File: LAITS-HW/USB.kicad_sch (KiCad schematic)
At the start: 27 parts, among them J201 USB_C_Receptacle_USB2.0, Q201 PDTC114Y, Q202 PDTC114Y, Q203 NX7002AK, Q204 NX7002AK, U201 CP2102N-Axx-xQFN28

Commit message: generate IBOM
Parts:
- Q203, Q204: Place (none) -> DNP; Status DNP -> (none)
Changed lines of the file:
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@@
       (effects (font (size 1.27 1.27)) hide)
     )
-    (property "Status" "DNP" (id 4) (at 274.955 123.19 0))
+    (property "Place" "DNP" (id 4) (at 274.955 123.19 0))
     (pin "1")
     (pin "2")
@@
       (effects (font (size 1.27 1.27)) hide)
     )
-    (property "Status" "DNP" (id 4) (at 250.825 123.19 0))
-    (pin "1")
-    (pin "2")
+    (property "Place" "DNP" (id 4) (at 250.825 123.19 0))
+    (pin "1")
+    (pin "2")

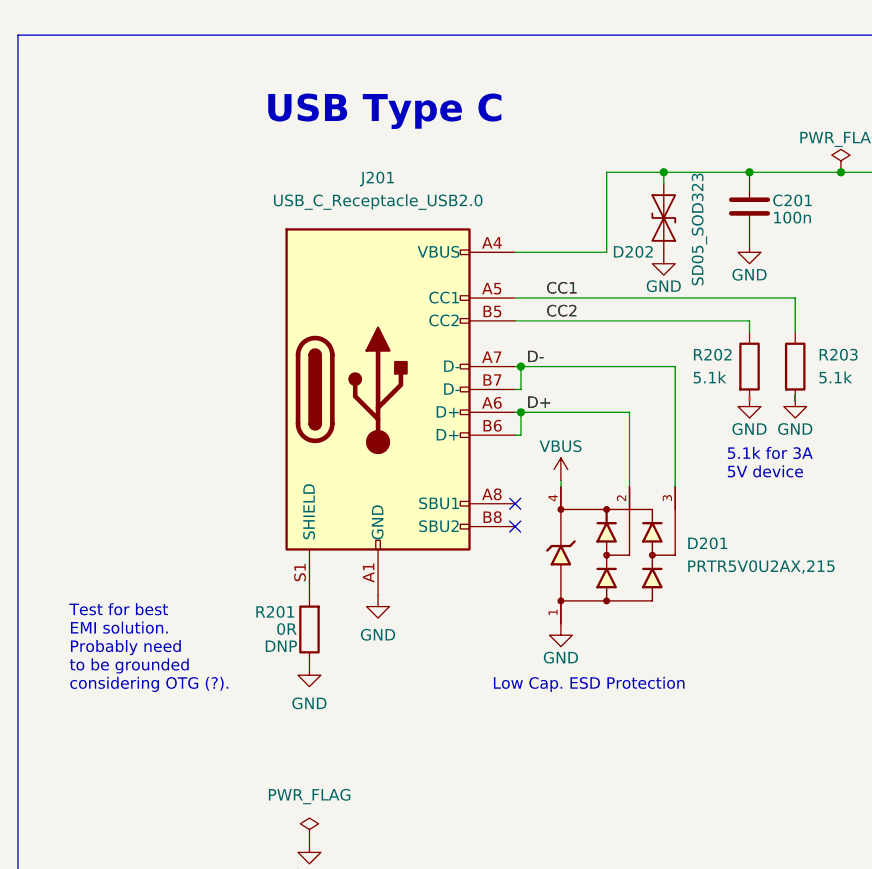
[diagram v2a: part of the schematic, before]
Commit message: Patch 1.0.1
Bug:

 - Changed U602 footprint from TSOT26 to SOT563 in order to reflect pin assignment.

Small bugs:

 - Missing silkscreen for SMD leds info (3V3, RX, TX)
 - DS18B20 silkscreen now reflect horizontal placement
 - Rotated and modified the pinout of the jumper JP603 so now it's clear that it is connected different in respect to JP601, JP602, JP604
 - Made visible the dot for the placement of U602
 - Made visible dot for placement D603 and D605
 - Added I2C info on Silkscreen for I2C Pull-up resistors
 - Add info on Sch for USB-C Shield connection
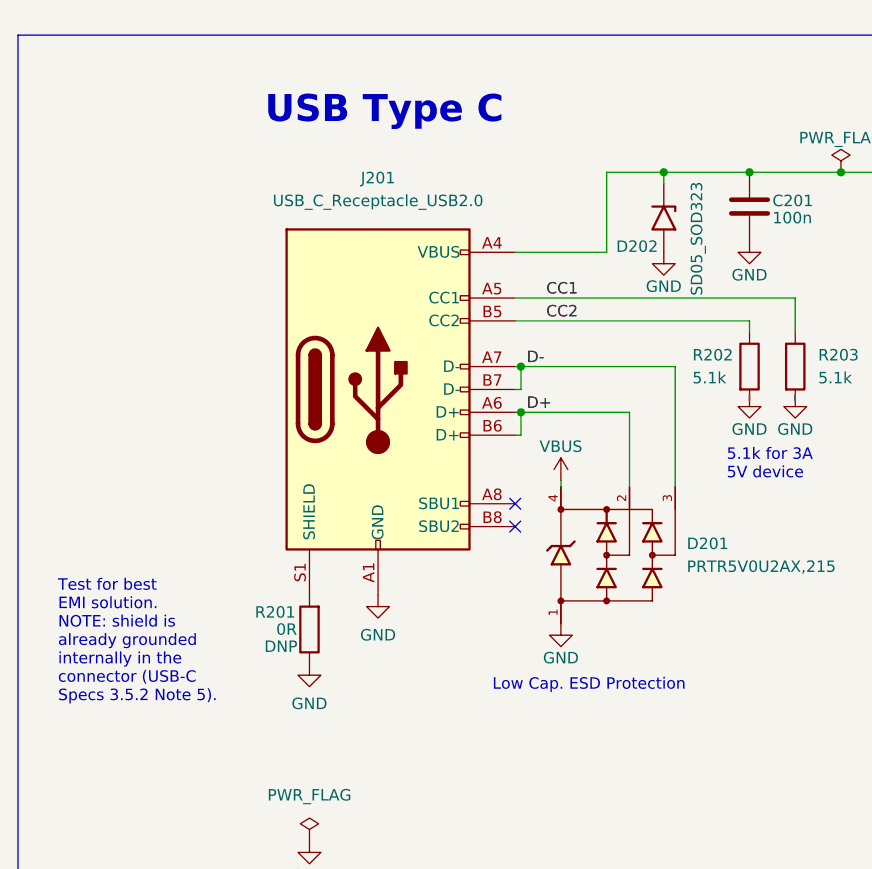
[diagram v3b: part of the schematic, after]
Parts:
- D202: symbol Diode:SD05_SOD323 -> Diode:SM6T100A
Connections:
- net GND: now also D202.2 (A2); no longer D202.1 (A1)
- net VBUS: now also D202.1 (A1); no longer D202.2 (A2)
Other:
- note added: "Test for best EMI solution. NOTE: shield is already grounded internally in the connector (USB-C Specs 3.5.2 Note 5)."
- note removed: "Test for best EMI solution. Probably need to be grounded considering OTG (?)."
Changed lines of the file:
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@@
     (title "PS + USB")
     (date "2022-07-14")
-    (rev "1.0")
+    (rev "1.0.1")
     (company "Simone Tollardo")
   )
@@
     )
   )
-  (text "Test for best\nEMI solution.\nProbably need\nto be grounded\nconsidering OTG (?)."
-    (at 23.495 126.365 0)
+  (text "Test for best\nEMI solution.\nNOTE: shield is \nalready grounded\ninternally in the \nconnector (USB-C\nSpecs 3.5.2 Note 5)."
+    (at 22.225 127.635 0)
     (effects (font (size 1.27 1.27)) (justify left bottom))
   )
@@
     (pin "1")
   )
-  (symbol (lib_id "Diode:SD05_SOD323") (at 89.535 73.66 90) (unit 1)
+  (symbol (lib_id "Diode:SM6T100A") (at 89.535 73.66 270) (unit 1)
     (in_bom yes) (on_board yes)
-    (property "Reference" "D202" (id 0) (at 83.82 77.47 90)
+    (property "Reference" "D202" (id 0) (at 88.9 76.835 90)
       (effects (font (size 1.27 1.27)) (justify right))
     )
-    (property "Value" "SD05_SOD323" (id 1) (at 93.345 68.58 0)
+    (property "Value" "SD05_SOD323" (id 1) (at 93.218 82.296 0)
       (effects (font (size 1.27 1.27)) (justify right))
     )
-    (property "Footprint" "Diode_SMD:D_SOD-323" (id 2) (at 94.615 73.66 0)
-      (effects (font (size 1.27 1.27)) hide)
-    )
+    (property "Footprint" "Diode_SMD:D_SOD-323" (id 2) (at 84.455 73.66 0)
+      (effects (font (size 1.27 1.27)) hide)
+    )
